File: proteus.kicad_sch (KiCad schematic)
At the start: 12 parts, among them J1 Conn_01x01, J15 Sicma_56, J2 Conn_01x01, J3 Conn_01x01

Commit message: update
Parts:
- removed F1, F2: Polyfuse, Resistor_SMD:R_1206_3216Metric, symbol Device:Polyfuse
- added F3, F4, F5, F6, F7, F8: Polyfuse, Resistor_SMD:R_1206_3216Metric, symbol Device:Polyfuse
- added J4: Conn_01x03, Connector_PinHeader_2.54mm:PinHeader_1x03_P2.54mm_Vertical, symbol Connector_Generic:Conn_01x03
- added J5: Conn_01x05, Connector_PinHeader_2.54mm:PinHeader_1x05_P2.54mm_Vertical, symbol Connector_Generic:Conn_01x05
- added JP3 (x2): Jumper_3_Bridged12, Jumper:SolderJumper-3_P1.3mm_Bridged12_RoundedPad1.0x1.5mm, symbol Jumper:Jumper_3_Bridged12
- added R25, R4: R_Small, Resistor_SMD:R_0805_2012Metric, symbol Device:R_Small
- H2: footprint MountingHole:MountingHole_4mm -> MountingHole:MountingHole_4mm_Pad_Via
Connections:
- net +5V: now also JP3.1 (A), R25.1
- net 12V_MR: now also J15.43, J15.44, J4.3 (Pin_3), JP3.3 (B), R4.1
- net 12V_RAW: now also J15.26
- net 5V_SENSOR_1: now also J15.45
- net AT1: now also J15.34
- net AT2: now also J15.49
- net AV1: now also J15.53
- net AV2: now also J15.51
- net AV3: now also J15.38
- net AV4: now also J15.52
- net AV5: now also J15.39
- net AV6: now also J15.37
- net AV7: now also J15.50
- net AV8: now also J15.36
- net AV9: now also J15.35
- net CAN+: now also J15.29
- net CAN-: now also J15.30
- net CAN2+: now also J15.31
- net CAN2-: now also J15.32
- net ETB1+: now also J15.28
- net ETB1-: now also J15.27
- net GND: now also J15.10, J15.21, J15.46, J15.48, J15.9, J5.5 (Pin_5)
- net IGN1: now also J15.1
- net IGN2: now also J15.2
- net IGN3: now also J15.3
- net IGN4: now also J15.4
- net IGN5: now also J15.5
- net IGN6: now also J15.6
- net IGN7: now also J15.7
- net IGN8: now also J15.8
- net KNOCK_1: now also J15.47
- net KNOCK_2: now also J15.33
- net LS1: now also J15.18
- net LS10: now also J15.20
- net LS11: now also F3.1, JP3.2 (C)
- net LS12: now also F4.1
- net LS13: now also F5.1
- net LS14: now also F6.1
- net LS15: now also F7.1
- net LS16: now also F8.1
- net LS2: now also J15.17
- net LS3: now also J15.16
- net LS4: now also J15.15
- net LS5: now also J15.22
- net LS6: now also J15.23
- net LS7: now also J15.24
- net LS8: now also J15.25
- net LS9: now also J15.19
- net lowside_uln2003-1/OUT7: now also J4.1 (Pin_1)
- net lowside_uln2003-1/OUT8: now also J4.2 (Pin_2)
- net LS11_F: now reaches J15.40
- net LS11_F: now also F3.2
- net LS15_F: now reaches J15.41
- net LS15_F: now also F7.2
- net LS13_F: now reaches J15.42
- net LS13_F: now also F5.2
- net LS12_F: now reaches J15.54
- net LS12_F: now also F4.2
- net LS16_F: now reaches J15.55
- net LS16_F: now also F8.2
- net LS14_F: now reaches J15.56
- net LS14_F: now also F6.2
- new net: JP3.3 (B), R25.2
- new net: JP3.1 (A), R4.2
- new net V_SUP: JP3.2 (C)
- new net quad_analog3/IN2: J5.3 (Pin_3)
- new net quad_analog3/IN3: J5.4 (Pin_4)
- new net quad_analog_temp/IN3: J5.2 (Pin_2)
- new net quad_analog_temp/IN4: J5.1 (Pin_1)
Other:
- sheet ign1 ports: added V_SUP; removed none
- sheet ign2 ports: added V_SUP; removed none
- sheet lowside_dual1 ports: added 12V_LED; removed none
- sheet lowside_quad1 ports: added 12V_LED; removed none
- sheet lowside_quad2 ports: added 12V_LED; removed none
- sheet mcu ports: added AT3, AT4, AV10, AV11, LS17, LS18; removed none
- sheet psu ports: added 12V_MR; removed none
- sheet quad_analog3 ports: added IN2, IN3, IN4, OUT2, OUT3, OUT4; removed none
- sheet quad_analog_temp ports: added IN3, IN4, OUT3, OUT4; removed none
- note added: "Igniter Voltage Select"
- note added: "Tacho Pullup"
- moved on the sheet: C1

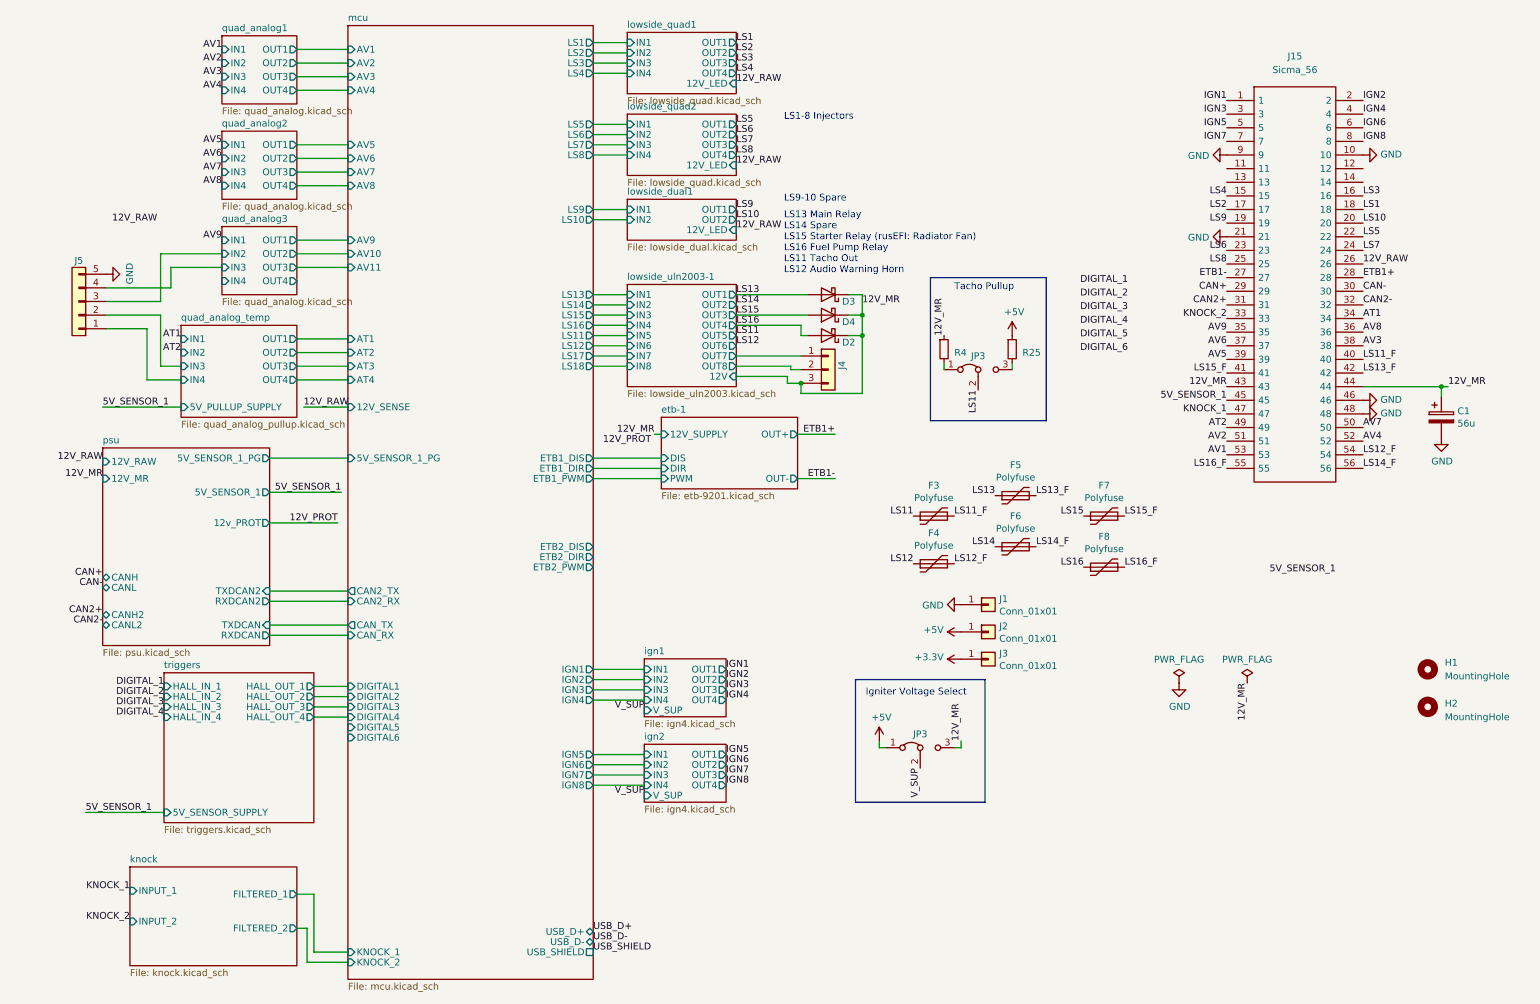
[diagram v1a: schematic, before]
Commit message: Updates - Route digital inputs to connector - Add optional VR conditioner - Second Enable for H-Bridge
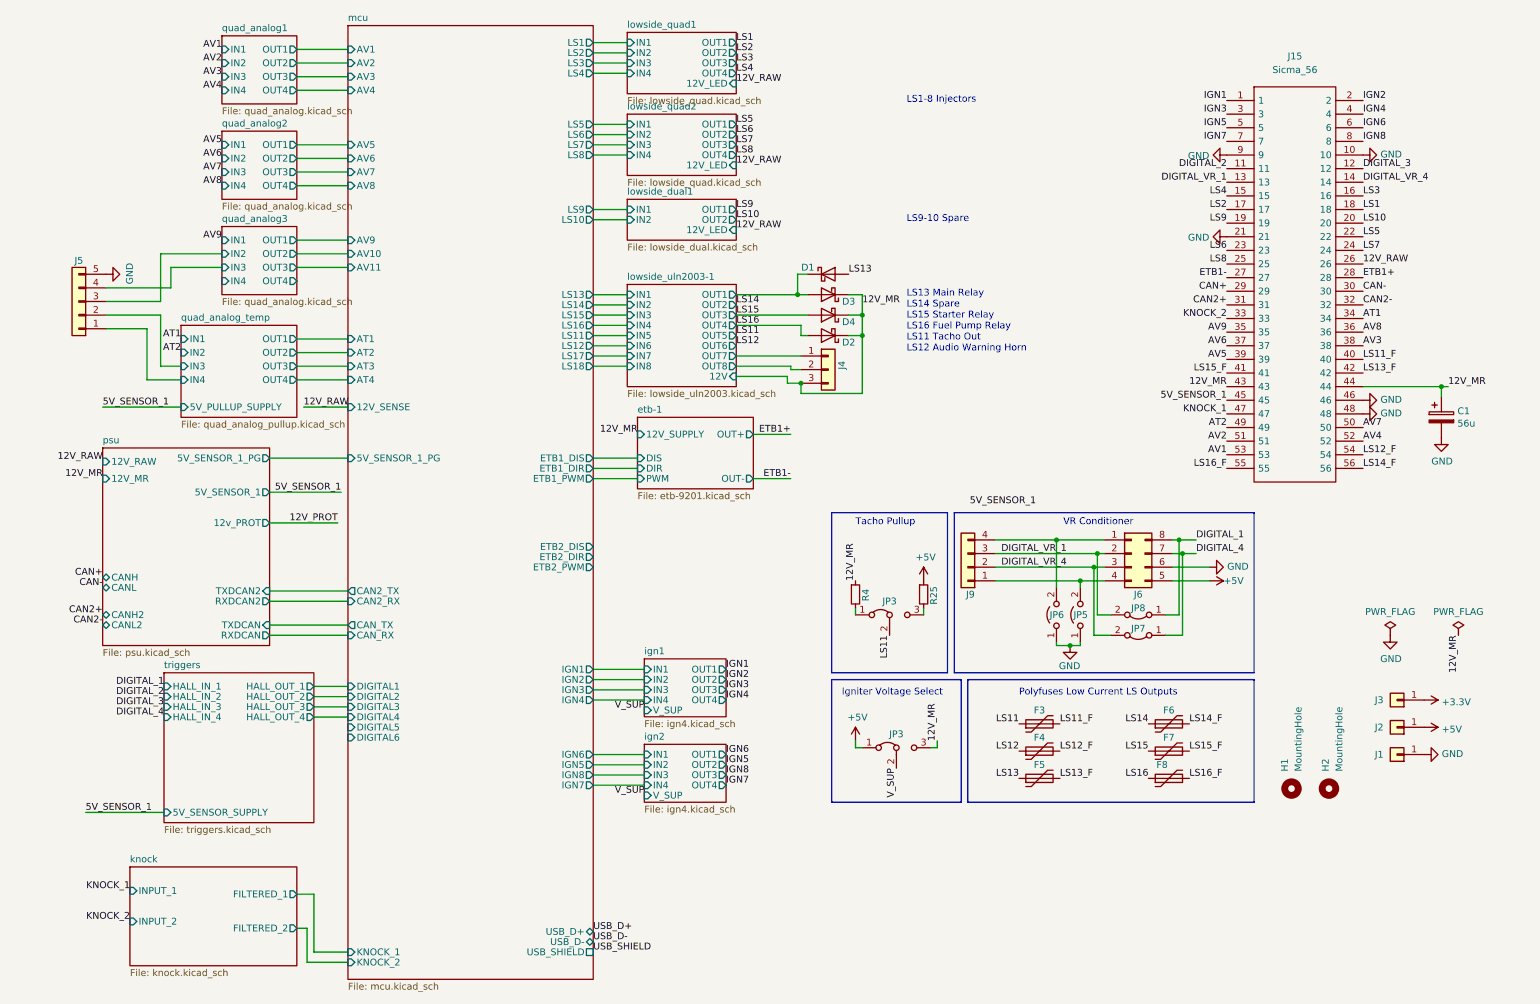
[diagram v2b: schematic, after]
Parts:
- added D1: D_Schottky, Diode_SMD:D_SMA, symbol Device:D_Schottky
- added J6: Conn_02x04_Counter_Clockwise, Package_DIP:DIP-8_W7.62mm, symbol Connector_Generic:Conn_02x04_Counter_Clockwise
- added J9: Conn_01x04, Connector_PinHeader_2.54mm:PinHeader_1x04_P2.54mm_Vertical, symbol Connector_Generic:Conn_01x04
- added JP5, JP6: Jumper_2_Bridged, Jumper:SolderJumper-2_P1.3mm_Open_RoundedPad1.0x1.5mm, symbol Jumper:Jumper_2_Open
- added JP7, JP8: Jumper_2_Bridged, Jumper:SolderJumper-2_P1.3mm_Bridged_RoundedPad1.0x1.5mm, symbol Jumper:Jumper_2_Bridged
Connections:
- net +5V: now also J6.5 (Pin_5)
- net DIGITAL_1: now also J6.8 (Pin_8), JP8.1 (A)
- net DIGITAL_2: now also J15.11
- net DIGITAL_3: now also J15.12
- net DIGITAL_4: now also J6.7 (Pin_7), JP7.1 (A)
- net GND: now also J6.6 (Pin_6), JP5.1 (A), JP6.1 (A)
- net LS13: now also D1.2 (A); no longer D3.2 (A)
- net DIGITAL_VR_1: now reaches J15.13
- net DIGITAL_VR_1: now also J6.2 (Pin_2), J9.3 (Pin_3), JP8.2 (B)
- net DIGITAL_VR_4: now reaches J15.14
- net DIGITAL_VR_4: now also J6.3 (Pin_3), J9.2 (Pin_2), JP7.2 (B)
- new net: J6.1 (Pin_1), J9.4 (Pin_4), JP6.2 (B)
- new net: J6.4 (Pin_4), J9.1 (Pin_1), JP5.2 (B)
- new net lowside_uln2003-1/OUT1: D1.1 (K), D3.2 (A)
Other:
- note added: "LS13 Main Relay LS14 Spare LS15 Starter Relay LS16 Fuel Pump Relay LS11 Tacho Out LS12 Audio Warning Horn"
- note added: "Polyfuses Low Current LS Outputs"
- note added: "VR Conditioner"
- note removed: "LS13 Main Relay LS14 Spare LS15 Starter Relay (rusEFI: Radiator Fan) LS16 Fuel Pump Relay LS11 Tacho Out LS12 Audio Warning Horn"
- moved on the sheet: F3, F4, F5, F6, F7, F8, H1, H2, J1, J2, J3, JP3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

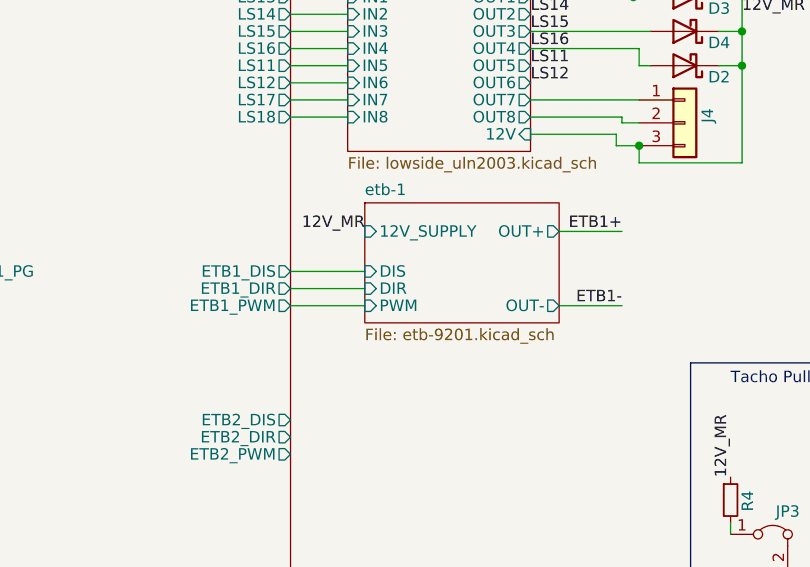
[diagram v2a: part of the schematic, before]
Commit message: Added ETB1_VSO and ETB1_ERR
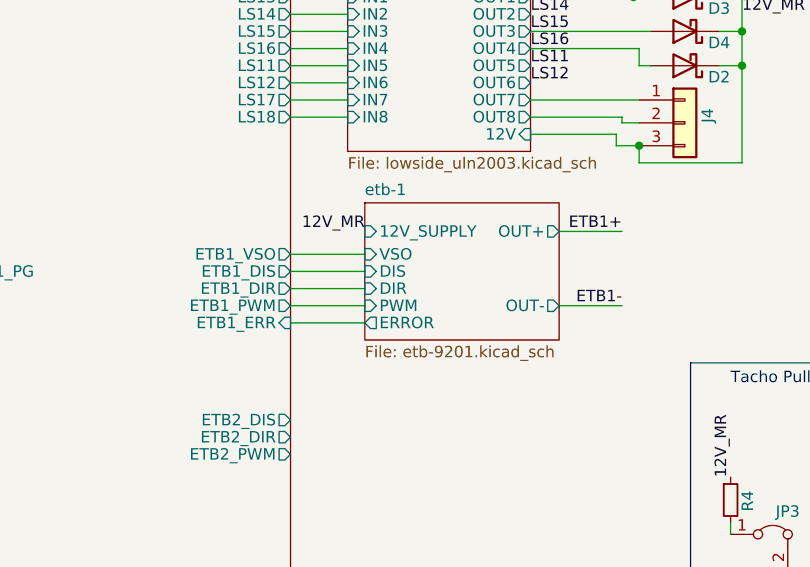
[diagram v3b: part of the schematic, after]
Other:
- sheet etb-1 ports: added ERROR, VSO; removed none
- sheet mcu ports: added ETB1_ERR, ETB1_VSO; removed none
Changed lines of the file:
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@@
+    (stroke (width 0) (type default))
+  )
+  (wire (pts (xy 114.3 95.885) (xy 122.555 95.885))
     (stroke (width 0) (type default))
   )
@@
   )
   (wire (pts (xy 205.105 132.715) (xy 203.2 132.715))
+    (stroke (width 0) (type default))
+  )
+  (wire (pts (xy 114.3 103.505) (xy 122.555 103.505))
     (stroke (width 0) (type default))
   )
@@
       (effects (font (size 1.27 1.27)) (justify right))
     )
+    (pin "ETB1_VSO" output (at 114.3 95.885 0)
+      (effects (font (size 1.27 1.27)) (justify right))
+    )
+    (pin "ETB1_ERR" input (at 114.3 103.505 0)
+      (effects (font (size 1.27 1.27)) (justify right))
+    )
     (instances
       (project "proteus"
@@
     )
   )
-  (sheet (at 122.555 90.17) (size 21.59 13.335) (fields_autoplaced)
+  (sheet (at 122.555 90.17) (size 21.59 15.24) (fields_autoplaced)
     (stroke (width 0) (type solid))
     (fill (color 0 0 0 0.0000))
@@
       (effects (font (size 1.27 1.27)) (justify left bottom))
     )
-    (property "Sheetfile" "etb-9201.kicad_sch" (at 122.555 104.0896 0)
+    (property "Sheetfile" "etb-9201.kicad_sch" (at 122.555 105.9946 0)
       (effects (font (size 1.27 1.27)) (justify left top))
     )
@@
       (effects (font (size 1.27 1.27)) (justify left))
     )
+    (pin "VSO" input (at 122.555 95.885 180)
+      (effects (font (size 1.27 1.27)) (justify left))
+    )
+    (pin "ERROR" output (at 122.555 103.505 180)
+      (effects (font (size 1.27 1.27)) (justify left))
+    )
